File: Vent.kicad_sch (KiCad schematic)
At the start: 11 parts, among them J2 B2B-XH-A_LF__SN_, J3 Conn_01x03_Pin, SW1 SW_Push, U1 ESP32-H2-MINI-1-H2

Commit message: feat: Add metadata and version to sheets
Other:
- title: (none) -> Vent
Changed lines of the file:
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@@
 	(generator_version "10.0")
 	(paper "A4")
+	(title_block
+		(title "Vent")
+		(date "2026-08-19")
+		(rev "v0.1.0")
+	)
 	(junction
 		(at 259.08 77.47)
@@
 		)
 		(instances
-			(project "Vynte PCB"
+			(project "Vent"
 				(path "/44080430-3c3a-4a58-87da-65c26034d41d"
 					(reference "#PWR014")
@@
 		)
 		(instances
-			(project "Vynte PCB"
+			(project "Vent"
 				(path "/44080430-3c3a-4a58-87da-65c26034d41d"
 					(reference "D1")
@@
 		)
 		(instances
-			(project "Vynte PCB"
+			(project "Vent"
 				(path "/44080430-3c3a-4a58-87da-65c26034d41d"
 					(reference "#PWR016")
@@
 		)
 		(instances
-			(project "Vynte PCB"
+			(project "Vent"
 				(path "/44080430-3c3a-4a58-87da-65c26034d41d"
 					(reference "#PWR04")
@@
 		)
 		(instances
-			(project "Vynte PCB"
+			(project "Vent"
 				(path "/44080430-3c3a-4a58-87da-65c26034d41d"
 					(reference "J3")
@@
 		)
 		(instances
-			(project "Vynte PCB"
+			(project "Vent"
 				(path "/44080430-3c3a-4a58-87da-65c26034d41d"
 					(reference "R7")
@@
 		)
 		(instances
-			(project "Vynte PCB"
+			(project "Vent"
 				(path "/44080430-3c3a-4a58-87da-65c26034d41d"
 					(reference "R5")
@@
 		)
 		(instances
-			(project "Vynte PCB"
+			(project "Vent"
 				(path "/44080430-3c3a-4a58-87da-65c26034d41d"
 					(reference "SW1")
@@
 		)
 		(instances
-			(project "Vynte PCB"
+			(project "Vent"
 				(path "/44080430-3c3a-4a58-87da-65c26034d41d"
 					(reference "#PWR019")
@@
 		)
 		(instances
-			(project "Vynte PCB"
+			(project "Vent"
 				(path "/44080430-3c3a-4a58-87da-65c26034d41d"
 					(reference "#PWR011")
@@
 		)
 		(instances
-			(project "Vynte PCB"
+			(project "Vent"
 				(path "/44080430-3c3a-4a58-87da-65c26034d41d"
 					(reference "R6")
@@
 		)
 		(instances
-			(project "Vynte PCB"
+			(project "Vent"
 				(path "/44080430-3c3a-4a58-87da-65c26034d41d"
 					(reference "C5")
@@
 		)
 		(instances
-			(project "Vynte PCB"
+			(project "Vent"
 				(path "/44080430-3c3a-4a58-87da-65c26034d41d"
 					(reference "J2")
@@
 		)
 		(instances
-			(project "Vynte PCB"
+			(project "Vent"
 				(path "/44080430-3c3a-4a58-87da-65c26034d41d"
 					(reference "#PWR017")
@@
 		)
 		(instances
-			(project "Vynte PCB"
+			(project "Vent"
 				(path "/44080430-3c3a-4a58-87da-65c26034d41d"
 					(reference "H1")
@@
 		)
 		(instances
-			(project "Vynte PCB"
+			(project "Vent"
 				(path "/44080430-3c3a-4a58-87da-65c26034d41d"
 					(reference "U1")
@@
 		)
 		(instances
-			(project "Vynte PCB"
+			(project "Vent"
 				(path "/44080430-3c3a-4a58-87da-65c26034d41d"
 					(reference "H4")
@@
 		)
 		(instances
-			(project "Vynte PCB"
+			(project "Vent"
 				(path "/44080430-3c3a-4a58-87da-65c26034d41d"
 					(reference "#PWR02")
@@
 		)
 		(instances
-			(project "Vynte PCB"
+			(project "Vent"
 				(path "/44080430-3c3a-4a58-87da-65c26034d41d"
 					(reference "#PWR018")
@@
 		)
 		(instances
-			(project "Vynte PCB"
+			(project "Vent"
 				(path "/44080430-3c3a-4a58-87da-65c26034d41d"
 					(reference "#PWR01")
@@
 		)
 		(instances
-			(project "Vynte PCB"
+			(project "Vent"
 				(path "/44080430-3c3a-4a58-87da-65c26034d41d"
 					(page "3")
@@
 		)
 		(instances
-			(project "Vynte PCB"
+			(project "Vent"
 				(path "/44080430-3c3a-4a58-87da-65c26034d41d"
 					(page "2")
@@
 		)
 		(instances
-			(project "Vynte PCB"
+			(project "Vent"
 				(path "/44080430-3c3a-4a58-87da-65c26034d41d"
 					(page "4")

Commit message: Schematic Organization
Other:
- sheet ExternalAutoprogramming renamed ExternalAutoprogramming (Low-Profile Female)
- sheet ExternalAutoprogramming (Low-Profile Female) ports: added RX, TX; removed D+, D-
- moved on the sheet: C5, D1, H1, H4, J2, J3, R5, R6, R7, SW1, U1

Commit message: fix: Add company name to schematic sheets
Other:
- company: (none) -> Vynte
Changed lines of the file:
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@@
 		(date "2026-08-19")
 		(rev "${PROJECT_REV}")
+		(company "Vynte")
 	)
 	(junction

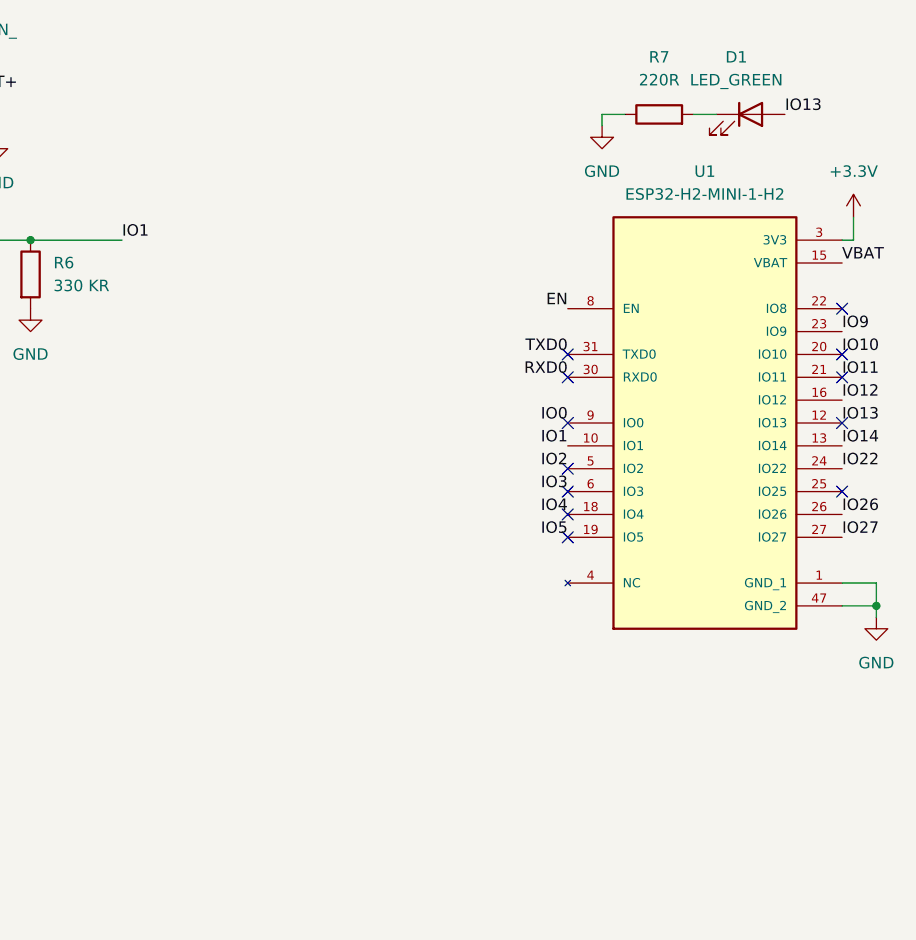
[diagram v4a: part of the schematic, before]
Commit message: feat: Change the ESP32 H2 symbol to be from PCM_Espressif
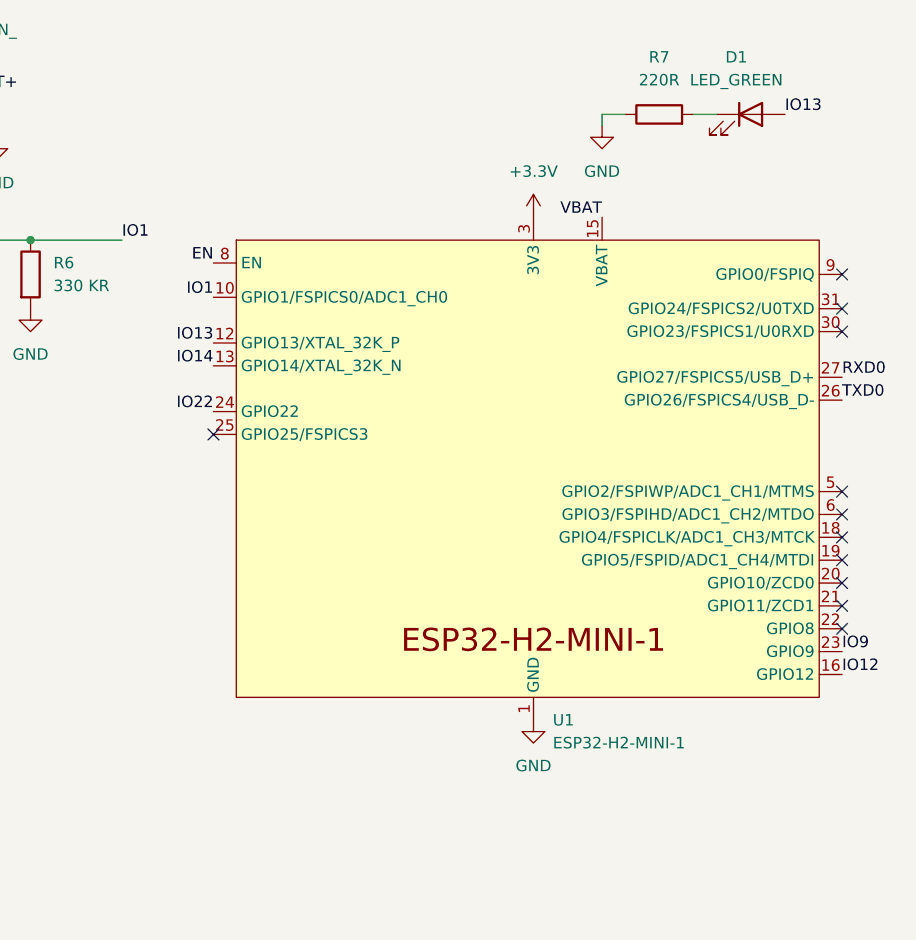
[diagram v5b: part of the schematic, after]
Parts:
- removed U1: ESP32-H2-MINI-1-H2, PCM_Espressif:ESP32-H2-MINI-1, symbol ESP32-H2-MINI-1-H2:ESP32-H2-MINI-1-H2
- added U1: ESP32-H2-MINI-1, PCM_Espressif:ESP32-H2-MINI-1, symbol PCM_Espressif:ESP32-H2-MINI-1
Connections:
- net +3.3V: now also U1.3 (3V3)
- net EN: now also U1.8 (EN)
- net GND: now also U1.1 (GND), U1.11 (GND), U1.14 (GND), U1.2 (GND), U1.36 (GND), U1.37 (GND), U1.38 (GND), U1.39 (GND), U1.40 (GND), U1.41 (GND), U1.42 (GND), U1.43 (GND), U1.44 (GND), U1.45 (GND), U1.46 (GND), U1.47 (GND), U1.48 (GND), U1.49 (GND), U1.50 (GND), U1.51 (GND), U1.52 (GND), U1.53 (GND)
- net IO1: now also U1.10 (GPIO1/FSPICS0/ADC1_CH0)
- net IO12: now also U1.16 (GPIO12)
- net IO13: now also U1.12 (GPIO13/XTAL_32K_P)
- net IO14: now also U1.13 (GPIO14/XTAL_32K_N)
- net IO22: now also U1.24 (GPIO22)
- net IO9: now also U1.23 (GPIO9)
- net RXD0: now also U1.27 (GPIO27/FSPICS5/USB_D+)
- net TXD0: now also U1.26 (GPIO26/FSPICS4/USB_D-)
- net VBAT: now also U1.15 (VBAT)
- no-connect marks 12 -> 11

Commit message: replace tx0 and rx0 with D+ and D-
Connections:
- net RXD0 renamed D+
- net TXD0 renamed D-
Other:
- sheet ExternalAutoprogramming (Low-Profile Female) ports: added D+, D-; removed RX, TX
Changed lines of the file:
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@@
 		)
 	)
-	(label "RXD0"
+	(label "D+"
 		(at 41.91 22.86 0)
 		(effects
@@
 		)
 	)
-	(label "TXD0"
+	(label "D-"
 		(at 41.91 25.4 0)
 		(effects
@@
 		)
 	)
-	(label "TXD0"
+	(label "D-"
 		(at 181.61 59.69 0)
 		(effects
@@
 		)
 	)
-	(label "RXD0"
+	(label "D+"
 		(at 181.61 57.15 0)
 		(effects
@@
 			)
 		)
-		(pin "RX" bidirectional
+		(pin "D+" bidirectional
 			(at 41.91 22.86 0)
 			(effects
@@
 			)
 		)
-		(pin "TX" bidirectional
+		(pin "D-" bidirectional
 			(at 41.91 25.4 0)
 			(effects

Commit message: metadata
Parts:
- C5: Digi-Key_PN (none) -> 311-1597-1-ND; MPN (none) -> CC0201KRX5R7BB104; Manufacturer (none) -> YAGEO
- D1: Digi-Key_PN (none) -> 732-5008-ND; MPN (none) -> 151031VS06000; Manufacturer (none) -> Würth Elektronik
- J2: Digi-Key_PN 455-2247-ND -> 455-B2B-XH-A-ND; MPN B2B-XH-A(LF)(SN) -> B2B-XH-A
- R5: Digi-Key_PN (none) -> 311-1MMCT-ND; MPN (none) -> RC0201FR-071ML; Manufacturer (none) -> YAGEO
- R6: Digi-Key_PN (none) -> YAG2603CT-ND; MPN (none) -> RC0201FR-07330KL; Manufacturer (none) -> YAGEO
- R7: Digi-Key_PN (none) -> YAG2509CT-ND; MPN (none) -> RC0201FR-07220RL; Manufacturer (none) -> YAGEO
- SW1: Digi-Key_PN (none) -> CKN10502CT-ND; MPN (none) -> PTS810SJM250SMTR LFS; Manufacturer (none) -> C&K
- U1: Digi-Key_PN (none) -> 1965-ESP32-H2-MINI-1-H4SCT-ND; MPN (none) -> ESP32-H2-MINI-1-H4S; Manufacturer (none) -> Espressif Systems
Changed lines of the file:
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@@
+			)
+		)
+		(property "Digi-Key_PN" "732-5008-ND" (at 0 0 0)
+			(effects
+				(font
+					(size 1.27 1.27)
+				)
+				(hide yes)
+			)
+		)
+		(property "Manufacturer" "Würth Elektronik" (at 0 0 0)
+			(effects
+				(font
+					(size 1.27 1.27)
+				)
+				(hide yes)
+			)
+		)
+		(property "MPN" "151031VS06000" (at 0 0 0)
+			(effects
+				(font
+					(size 1.27 1.27)
+				)
+				(hide yes)
 			)
 		)
@@
 			)
 		)
+		(property "Digi-Key_PN" "YAG2509CT-ND" (at 0 0 0)
+			(effects
+				(font
+					(size 1.27 1.27)
+				)
+				(hide yes)
+			)
+		)
+		(property "Manufacturer" "YAGEO" (at 0 0 0)
+			(effects
+				(font
+					(size 1.27 1.27)
+				)
+				(hide yes)
+			)
+		)
+		(property "MPN" "RC0201FR-07220RL" (at 0 0 0)
+			(effects
+				(font
+					(size 1.27 1.27)
+				)
+				(hide yes)
+			)
+		)
 		(pin "2"
 		)
@@
 					(size 1.27 1.27)
 				)
+			)
+		)
+		(property "Digi-Key_PN" "311-1MMCT-ND" (at 0 0 0)
+			(effects
+				(font
+					(size 1.27 1.27)
+				)
+				(hide yes)
+			)
+		)
+		(property "Manufacturer" "YAGEO" (at 0 0 0)
+			(effects
+				(font
+					(size 1.27 1.27)
+				)
+				(hide yes)
+			)
+		)
+		(property "MPN" "RC0201FR-071ML" (at 0 0 0)
+			(effects
+				(font
+					(size 1.27 1.27)
+				)
+				(hide yes)
 			)
 		)
@@
 			)
 		)
+		(property "Digi-Key_PN" "CKN10502CT-ND" (at 0 0 0)
+			(effects
+				(font
+					(size 1.27 1.27)
+				)
+				(hide yes)
+			)
+		)
+		(property "Manufacturer" "C&K" (at 0 0 0)
+			(effects
+				(font
+					(size 1.27 1.27)
+				)
+				(hide yes)
+			)
+		)
+		(property "MPN" "PTS810SJM250SMTR LFS" (at 0 0 0)
+			(effects
+				(font
+					(size 1.27 1.27)
+				)
+				(hide yes)
+			)
+		)
 		(pin "2"
 		)
@@
 			)
 		)
+		(property "Digi-Key_PN" "1965-ESP32-H2-MINI-1-H4SCT-ND" (at 0 0 0)
+			(effects
+				(font
+					(size 1.27 1.27)
+				)
+				(hide yes)
+			)
+		)
+		(property "Manufacturer" "Espressif Systems" (at 0 0 0)
+			(effects
+				(font
+					(size 1.27 1.27)
+				)
+				(hide yes)
+			)
+		)
+		(property "MPN" "ESP32-H2-MINI-1-H4S" (at 0 0 0)
+			(effects
+				(font
+					(size 1.27 1.27)
+				)
+				(hide yes)
+			)
+		)
 		(pin "38"
 		)
@@
 			)
 		)
+		(property "Digi-Key_PN" "YAG2603CT-ND" (at 0 0 0)
+			(effects
+				(font
+					(size 1.27 1.27)
+				)
+				(hide yes)
+			)
+		)
+		(property "Manufacturer" "YAGEO" (at 0 0 0)
+			(effects
+				(font
+					(size 1.27 1.27)
+				)
+				(hide yes)
+			)
+		)
+		(property "MPN" "RC0201FR-07330KL" (at 0 0 0)
+			(effects
+				(font
+					(size 1.27 1.27)
+				)
+				(hide yes)
+			)
+		)
 		(pin "1"
 		)
@@
 			)
 		)
+		(property "Digi-Key_PN" "311-1597-1-ND" (at 0 0 0)
+			(effects
+				(font
+					(size 1.27 1.27)
+				)
+				(hide yes)
+			)
+		)
+		(property "Manufacturer" "YAGEO" (at 0 0 0)
+			(effects
+				(font
+					(size 1.27 1.27)
+				)
+				(hide yes)
+			)
+		)
+		(property "MPN" "CC0201KRX5R7BB104" (at 0 0 0)
+			(effects
+				(font
+					(size 1.27 1.27)
+				)
+				(hide yes)
+			)
+		)
 		(pin "1"
 		)
@@
 			)
 		)
-		(property "Digi-Key_PN" "455-2247-ND"
+		(property "Digi-Key_PN" "455-B2B-XH-A-ND"
 			(at 93.98 30.48 0)
 			(hide yes)
@@
 			)
 		)
-		(property "MPN" "B2B-XH-A(LF)(SN)"
+		(property "MPN" "B2B-XH-A"
 			(at 96.52 30.48 0)
 			(hide yes)
